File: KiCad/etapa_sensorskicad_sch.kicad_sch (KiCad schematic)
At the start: 12 parts, among them J1 Conn_01x04_Pin, J2 Conn_01x04_Pin, Q1 IRLIZ44N

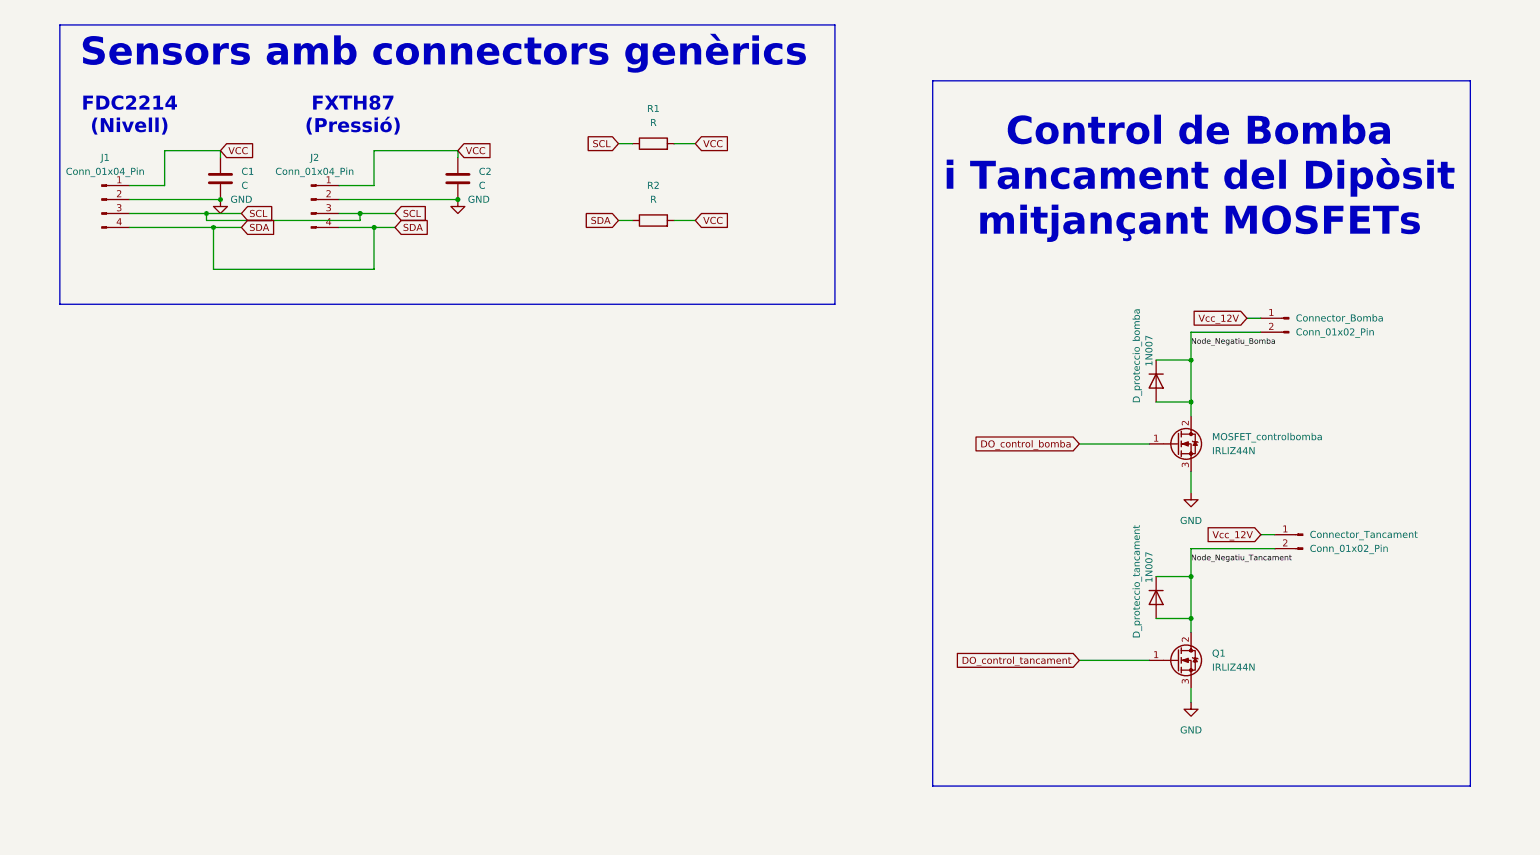
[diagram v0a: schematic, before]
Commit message: Hem afegit el simbol del sensor de nivell
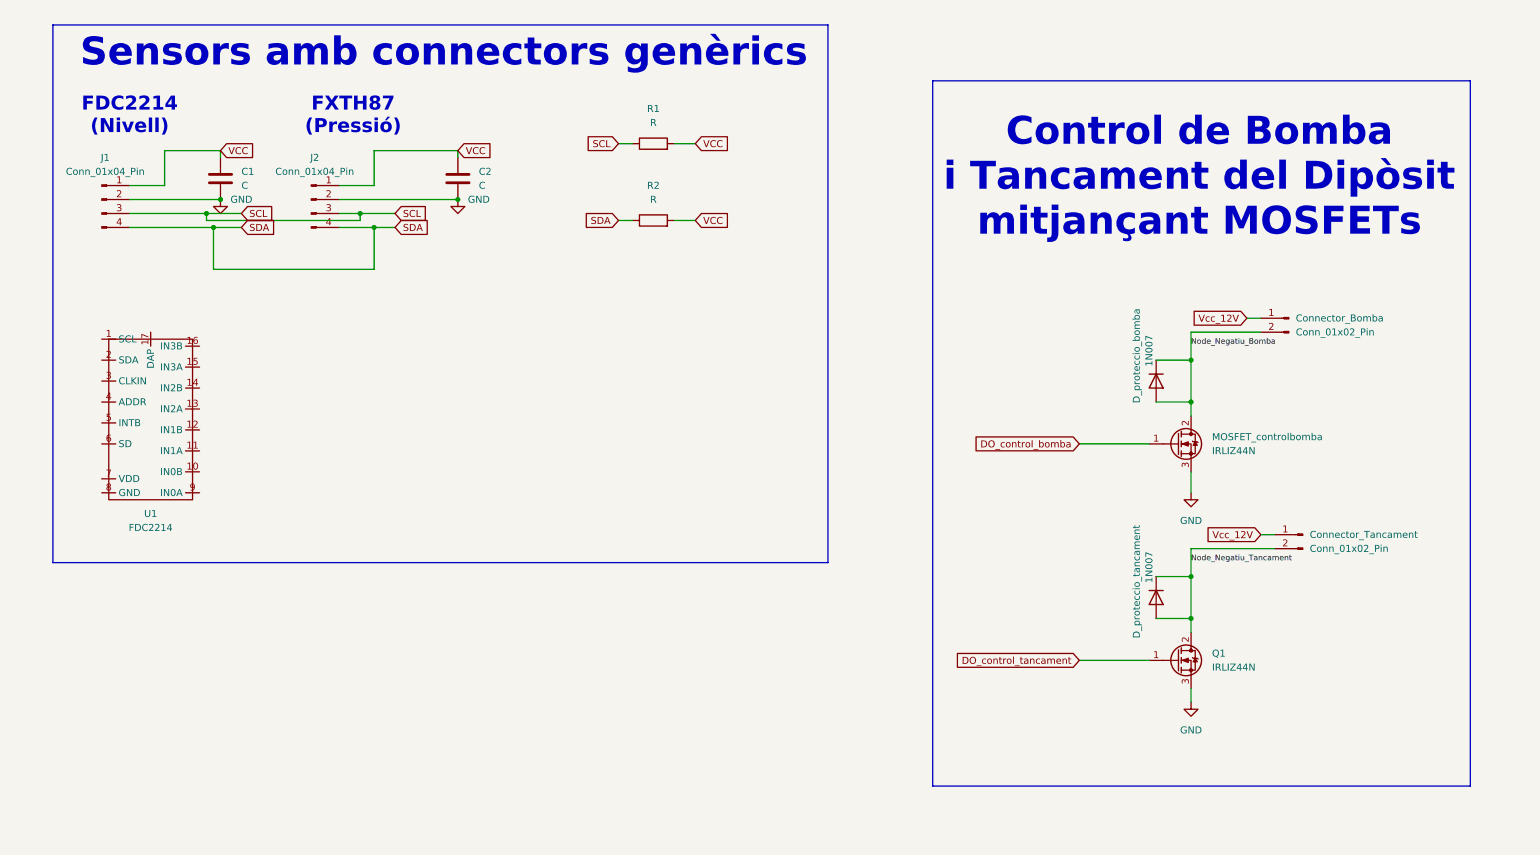
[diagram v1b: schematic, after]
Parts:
- added U1: FDC2214, symbol Sensors_Custom:FDC2214
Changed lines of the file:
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@@
 	(bus
 		(pts
-			(xy 162.56 16.51) (xy 162.56 67.31)
+			(xy 161.29 16.51) (xy 161.29 114.3)
 		)
 		(stroke
@@
 	(bus
 		(pts
-			(xy 21.59 16.51) (xy 162.56 16.51)
+			(xy 20.32 16.51) (xy 161.29 16.51)
 		)
 		(stroke
@@
 	(bus
 		(pts
-			(xy 21.59 16.51) (xy 21.59 67.31)
+			(xy 20.32 16.51) (xy 20.32 114.3)
 		)
 		(stroke
@@
 	(bus
 		(pts
-			(xy 162.56 67.31) (xy 21.59 67.31)
+			(xy 161.29 114.3) (xy 20.32 114.3)
 		)
 		(stroke
@@
 					(unit 1)
 				)
+			)
+		)
+	)
+	(symbol
+		(lib_id "Sensors_Custom:FDC2214")
+		(at 39.37 74.93 0)
+		(unit 1)
+		(exclude_from_sim no)
+		(in_bom yes)
+		(on_board yes)
+		(dnp no)
+		(fields_autoplaced yes)
+		(property "Reference" "U1"
+			(at 38.1 105.41 0)
+			(effects
+				(font
+					(size 1.27 1.27)
+				)
+			)
+		)
+		(property "Value" "FDC2214"
+			(at 38.1 107.95 0)
+			(effects
+				(font
+					(size 1.27 1.27)
+				)
+			)
+		)
+		(property "Footprint" ""
+			(at 39.37 74.93 0)
+			(effects
+				(font
+					(size 1.27 1.27)
+				)
+				(hide yes)
+			)
+		)
+		(property "Datasheet" ""
+			(at 39.37 74.93 0)
+			(effects
+				(font
+					(size 1.27 1.27)
+				)
+				(hide yes)
+			)
+		)
+		(property "Description" ""
+			(at 39.37 74.93 0)
+			(effects
+				(font
+					(size 1.27 1.27)
+				)
+				(hide yes)
+			)
+		)
+		(pin "6"
+		)
+		(pin "2"
+		)
+		(pin "5"
+		)
+		(pin "16"
+		)
+		(pin "3"
+		)
+		(pin "13"
+		)
+		(pin "9"
+		)
+		(pin "1"
+		)
+		(pin "4"
+		)
+		(pin "14"
+		)
+		(pin "8"
+		)
+		(pin "15"
+		)
+		(pin "7"
+		)
+		(pin "17"
+		)
+		(pin "12"
+		)
+		(pin "11"
+		)
+		(pin "10"
+		)
+		(instances
+			(project ""
+				(path "/27a7fca5-115a-450a-aa60-496c314f6c0e/214c85b5-e11a-40fa-b086-a325260ddb4b"
+					(reference "U1")
+					(unit 1)
+				)

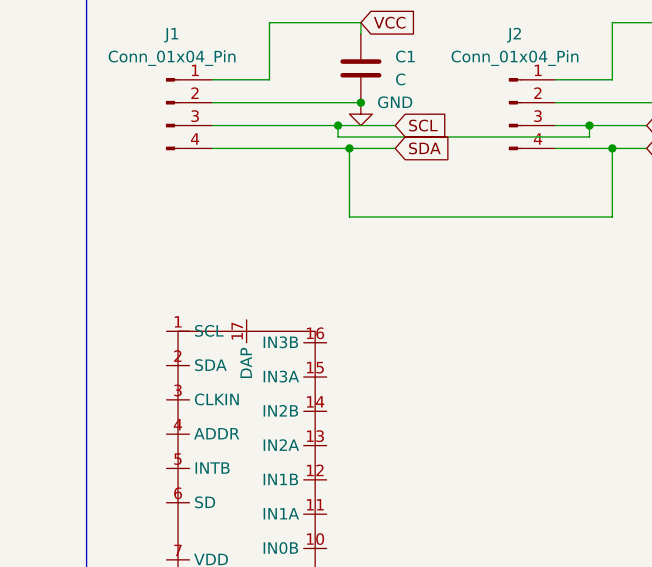
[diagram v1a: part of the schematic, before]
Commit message: Afegim el footprint que utilitzarem en text
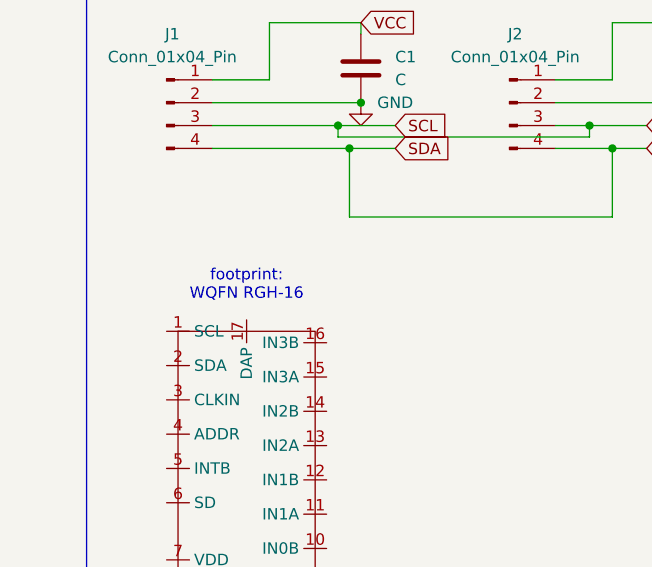
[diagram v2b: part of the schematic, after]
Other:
- note added: "footprint: WQFN RGH-16"
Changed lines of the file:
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@@
+		)
+	)
+	(text "footprint:\nWQFN RGH-16"
+		(exclude_from_sim no)
+		(at 38.1 68.58 0)
+		(effects
+			(font
+				(size 1.27 1.27)
+			)
 		)
 	)

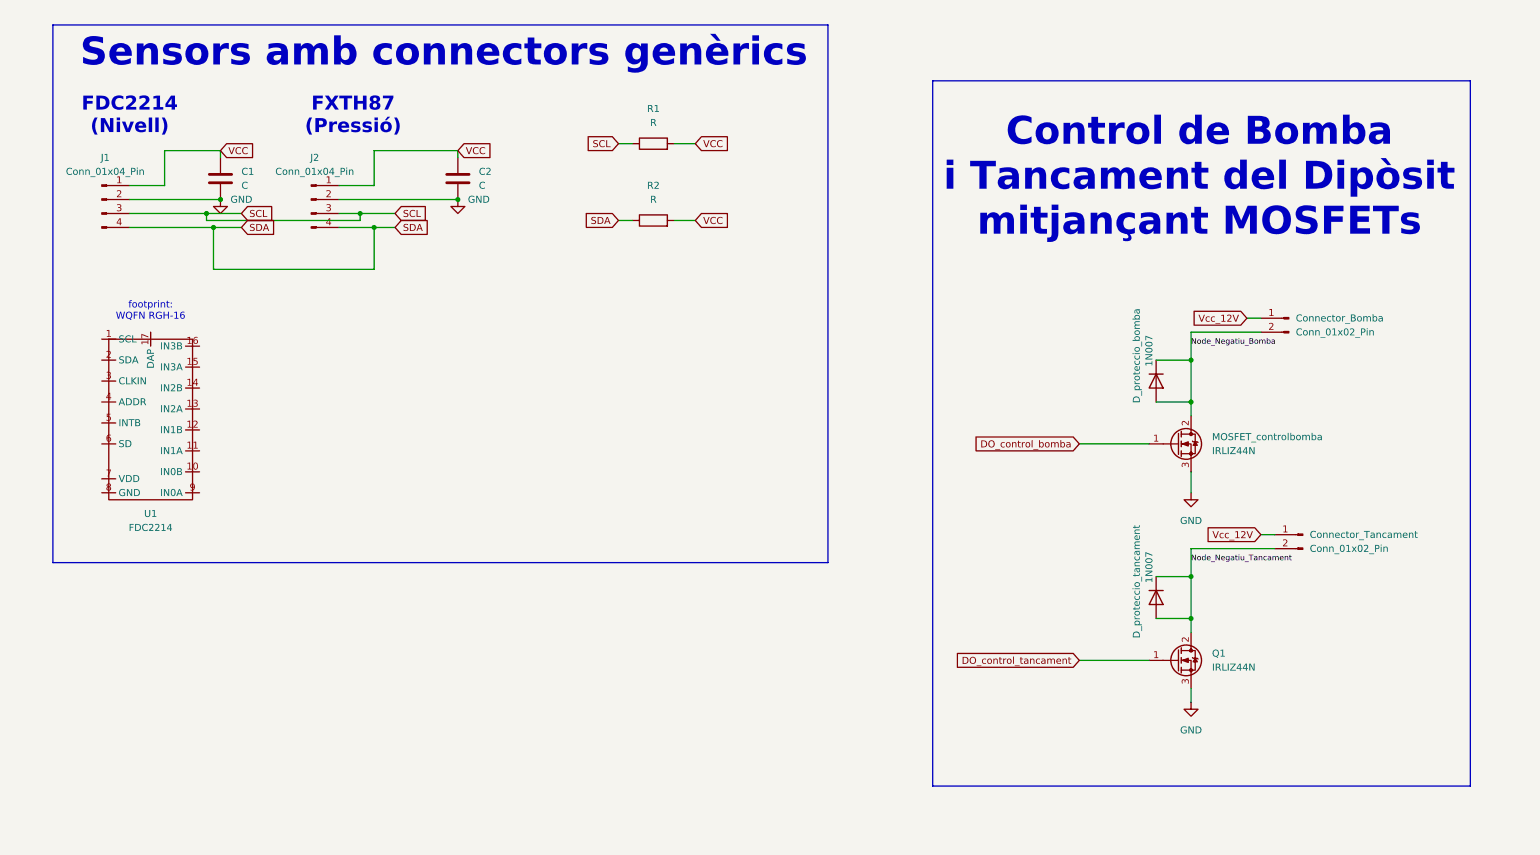
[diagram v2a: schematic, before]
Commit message: Relé posat per protegir el MOSFET i el micro
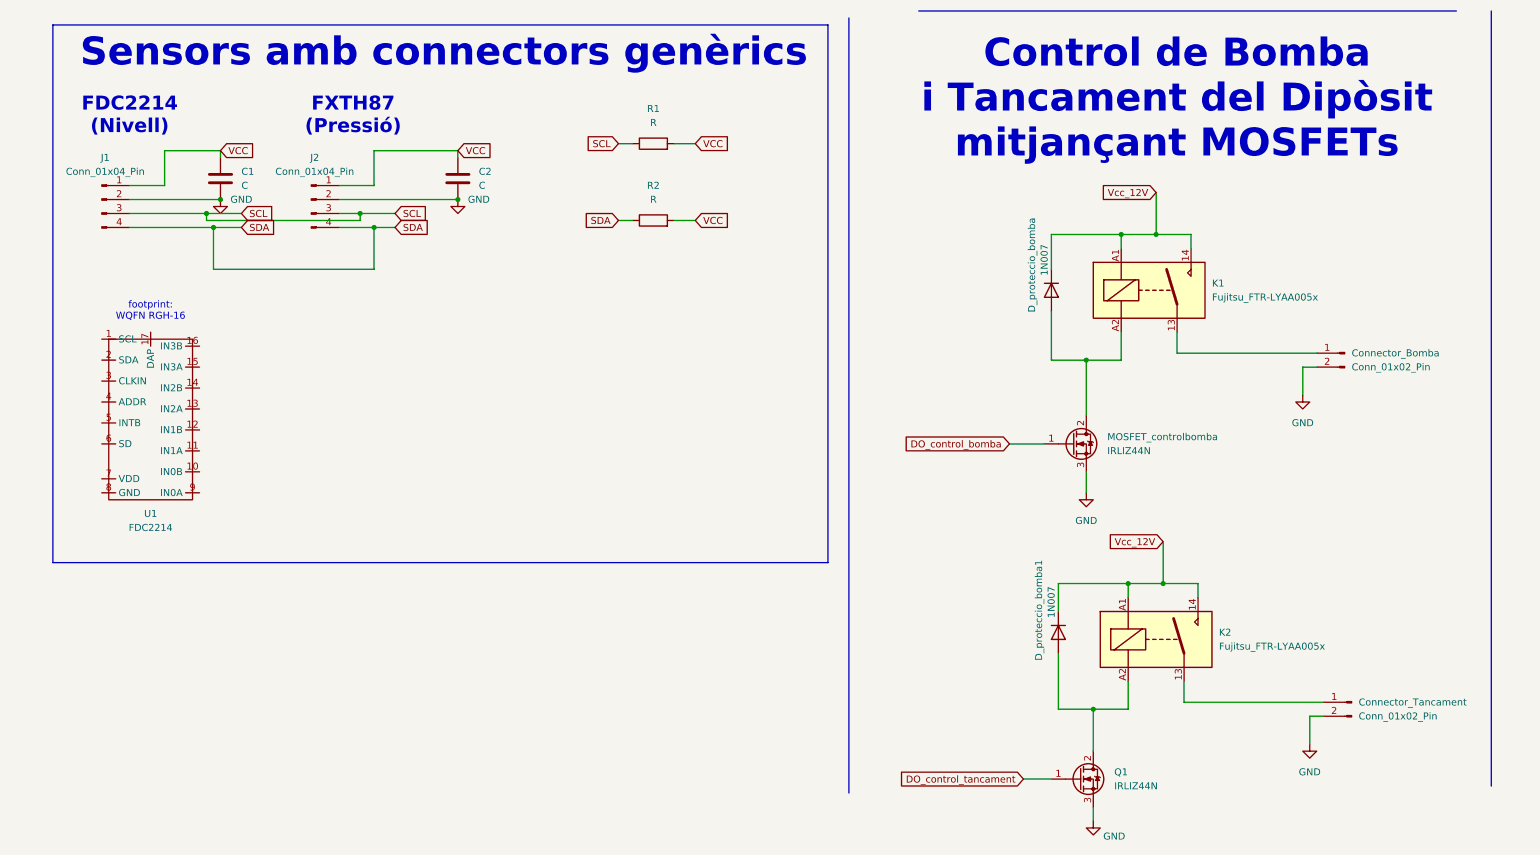
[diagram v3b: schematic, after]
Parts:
- removed D_proteccio_tancament: 1N007, symbol Device:D
- added D_proteccio_bomba1: 1N007, symbol Device:D
- added K1, K2: Fujitsu_FTR-LYAA005x, Relay_THT:Relay_SPST-NO_Fujitsu_FTR-LYAA005x_FormA_Vertical, symbol Relay:Fujitsu_FTR-LYAA005x
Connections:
- net GND: now also Connector_Bomba.2 (Pin_2), Connector_Tancament.2 (Pin_2)
- net Vcc_12V: now also D_proteccio_bomba.1 (K), D_proteccio_bomba1.1 (K), K1.14, K1.A1, K2.14, K2.A1; no longer Connector_Bomba.1 (Pin_1), Connector_Tancament.1 (Pin_1)
- net Node_Negatiu_Bomba: no longer names the net of D_proteccio_bomba.2 (A), MOSFET_controlbomba.2 (D)
- net Node_Negatiu_Bomba: now also K1.A2; no longer Connector_Bomba.2 (Pin_2), D_proteccio_bomba.1 (K)
- net Node_Negatiu_Tancament: no longer names the net of Q1.2 (D)
- net Node_Negatiu_Tancament: now also D_proteccio_bomba1.2 (A), K2.A2; no longer Connector_Tancament.2 (Pin_2)
- new net: Connector_Tancament.1 (Pin_1), K2.13
- new net: Connector_Bomba.1 (Pin_1), K1.13
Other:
- moved on the sheet: D_proteccio_bomba, MOSFET_controlbomba, Q1

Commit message: Afegim les conexions al primer simbol que vam crear i modifiquem les definicions dels pins (SCL/SDA en bidireccional)
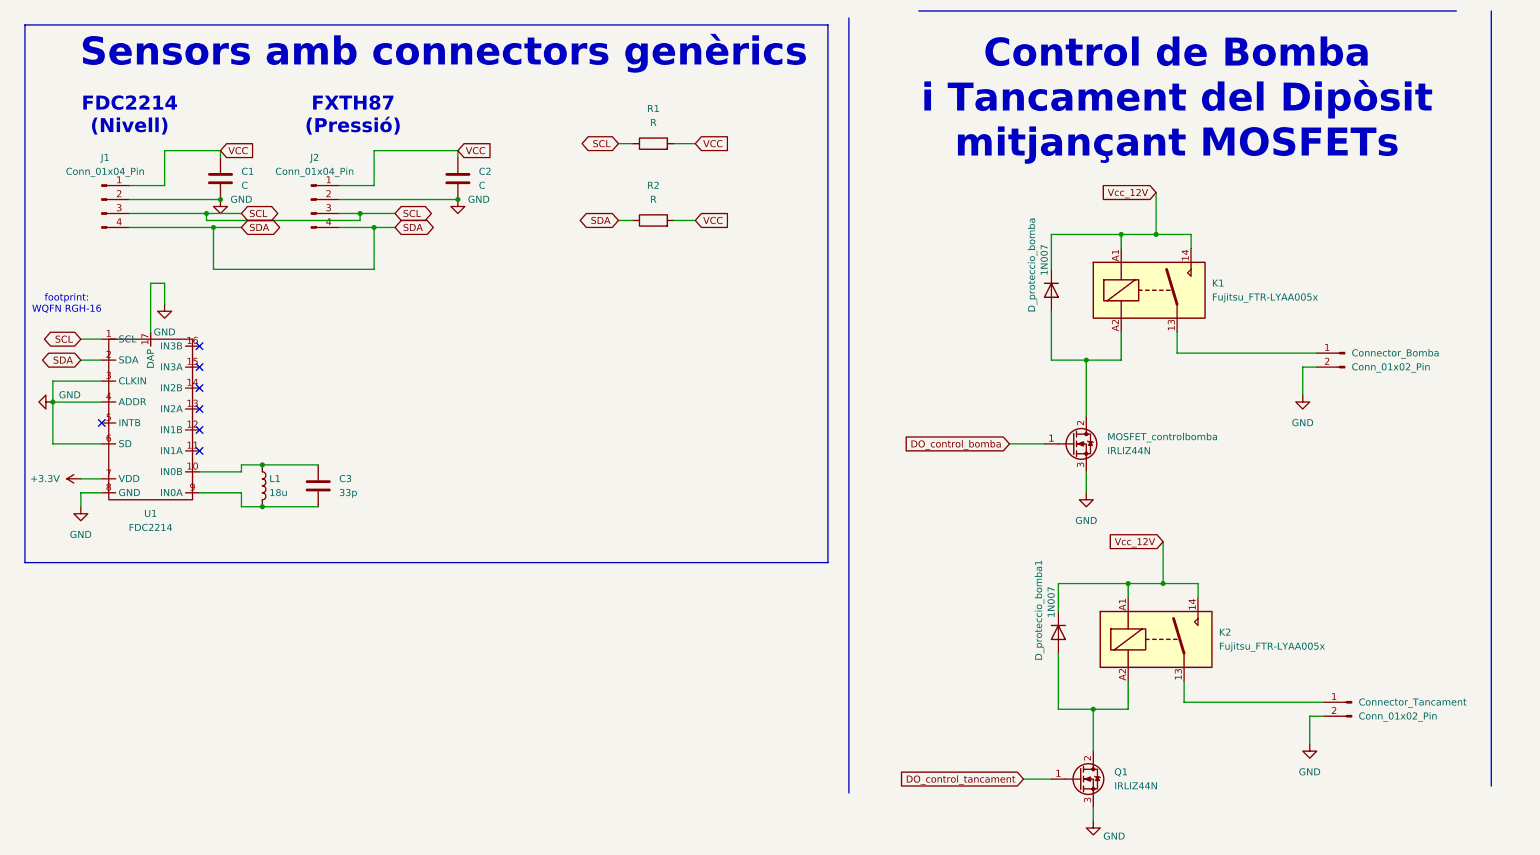
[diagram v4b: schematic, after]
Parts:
- added C3: 33p, symbol Device:C
- added L1: 18u, symbol Device:L
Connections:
- net GND: now also U1.17 (DAP), U1.3 (CLKIN), U1.4 (ADDR), U1.6 (SD), U1.8 (GND)
- net SCL: now also U1.1 (SCL)
- net SDA: now also U1.2 (SDA)
- net at U1.10 (IN0B): now also C3.1, L1.1
- net +3.3V: now reaches U1.7 (VDD)
- net at U1.9 (IN0A): now also C3.2, L1.2
- no-connect marks 0 -> 7
